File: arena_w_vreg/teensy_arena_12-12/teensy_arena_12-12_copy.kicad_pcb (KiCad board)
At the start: 4 copper layers, 254 x 254 mm, 87 parts, among them J1 Barrel_Jack, J2 Conn_01x04, J3 Conn_01x04, P1 CONN15, P10 CONN15, P11 CONN15, P12 CONN15, P2 CONN15, P3 CONN15, P4 CONN15, P5 CONN15, P6 CONN15, P7 CONN15, P8 CONN15, P9 CONN15, Q2 MOSFET_NCHAN, SW1 SW_SPDT, U1 TXB0108PW, U10 AZ1084-5.0, U11 AZ1084-5.0, U12 AZ1084-5.0, U13 AZ1084-5.0, U14 AZ1084-5.0, U15 AZ1084-5.0, U16 AZ1084-5.0, U17 AZ1084-5.0, U18 Teensy4.1, U2 TXB0108PW, U3 TXB0108PW, U4 TXB0108PW, U5 TXB0108PW, U6 AZ1084-5.0, U7 AZ1084-5.0, U8 AZ1084-5.0, U9 AZ1084-5.0

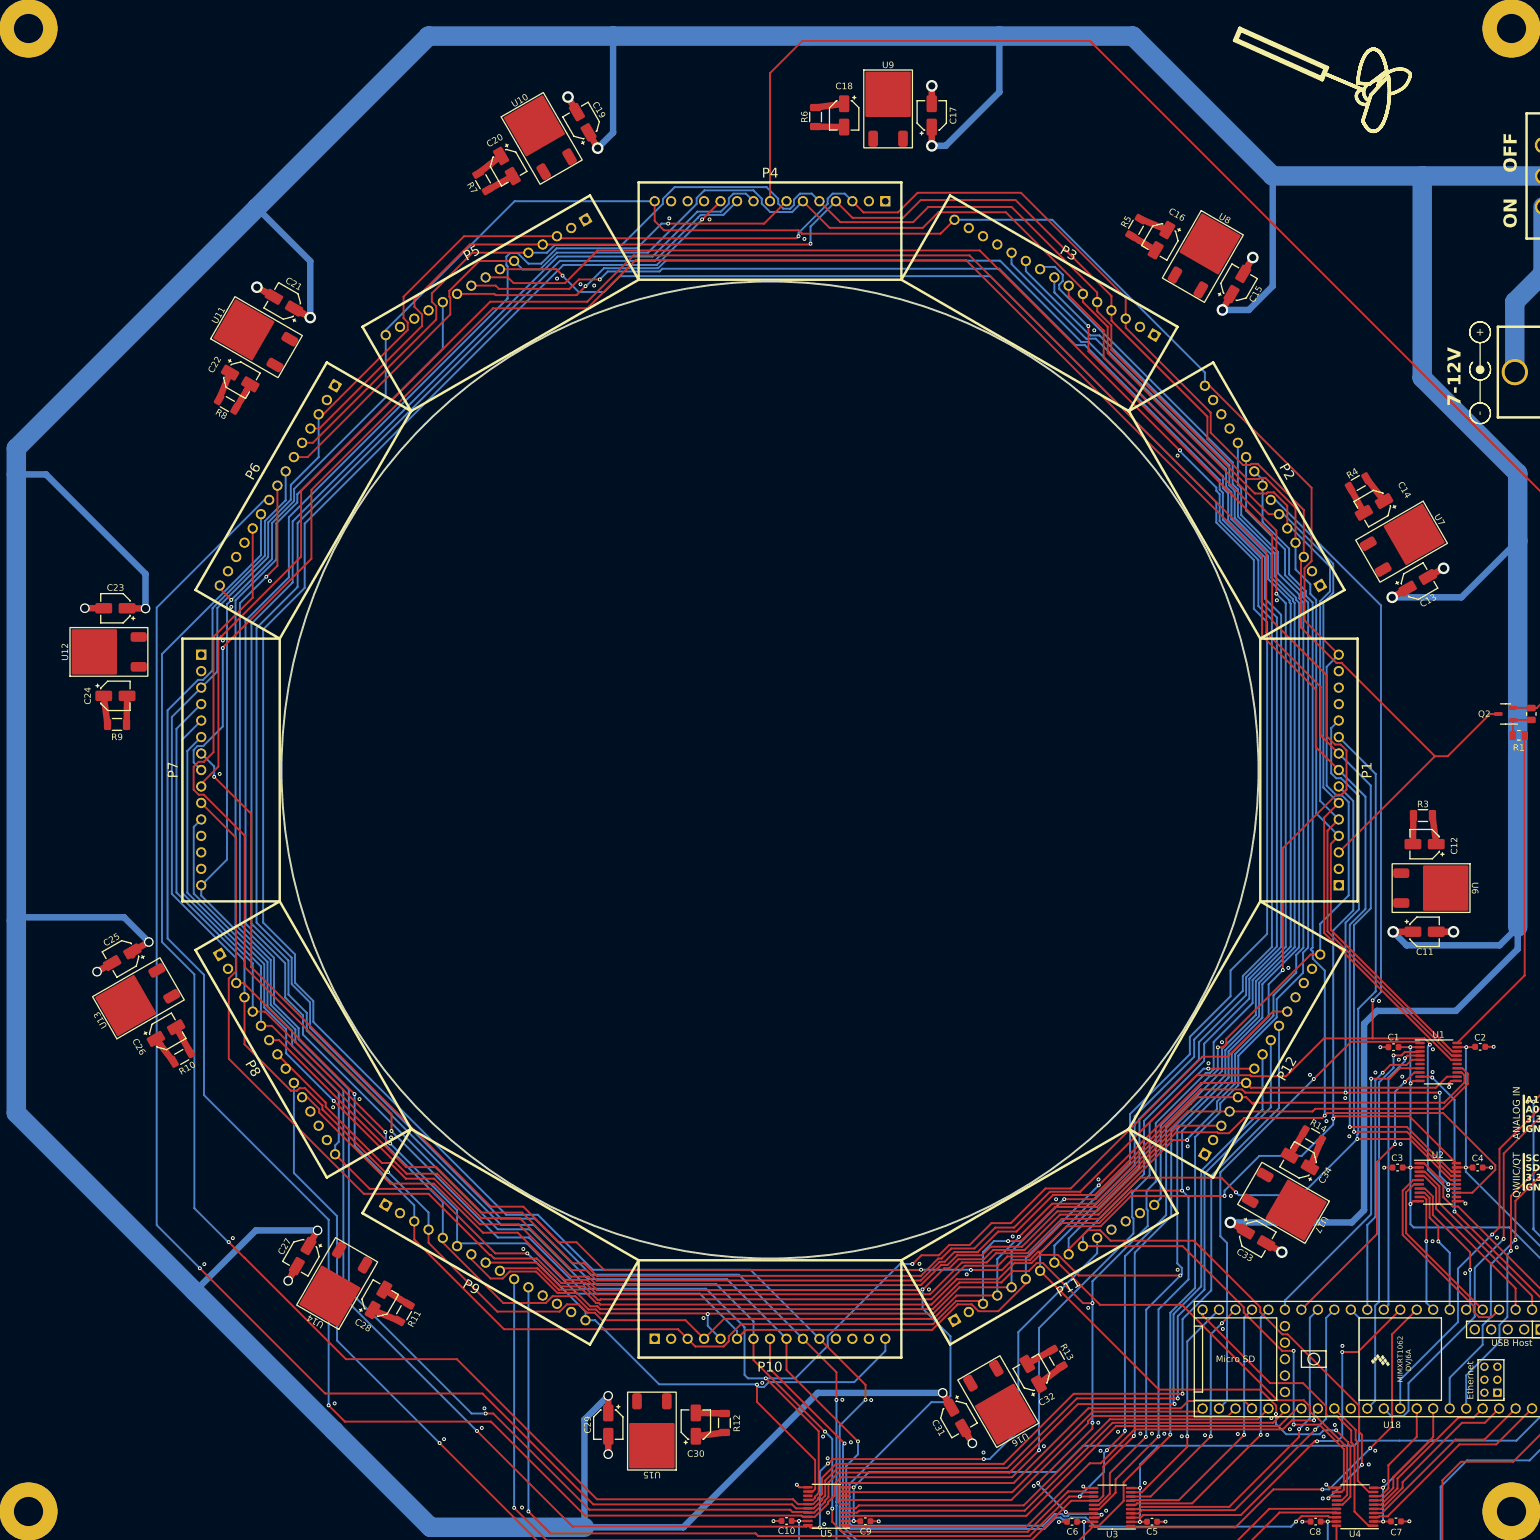
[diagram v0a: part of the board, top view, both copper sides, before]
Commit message: Fixed issue with AZ1084CD-5.0TRG1.
Note, need to do re-route the voltage regulators and redo the CPL file and gerber files.
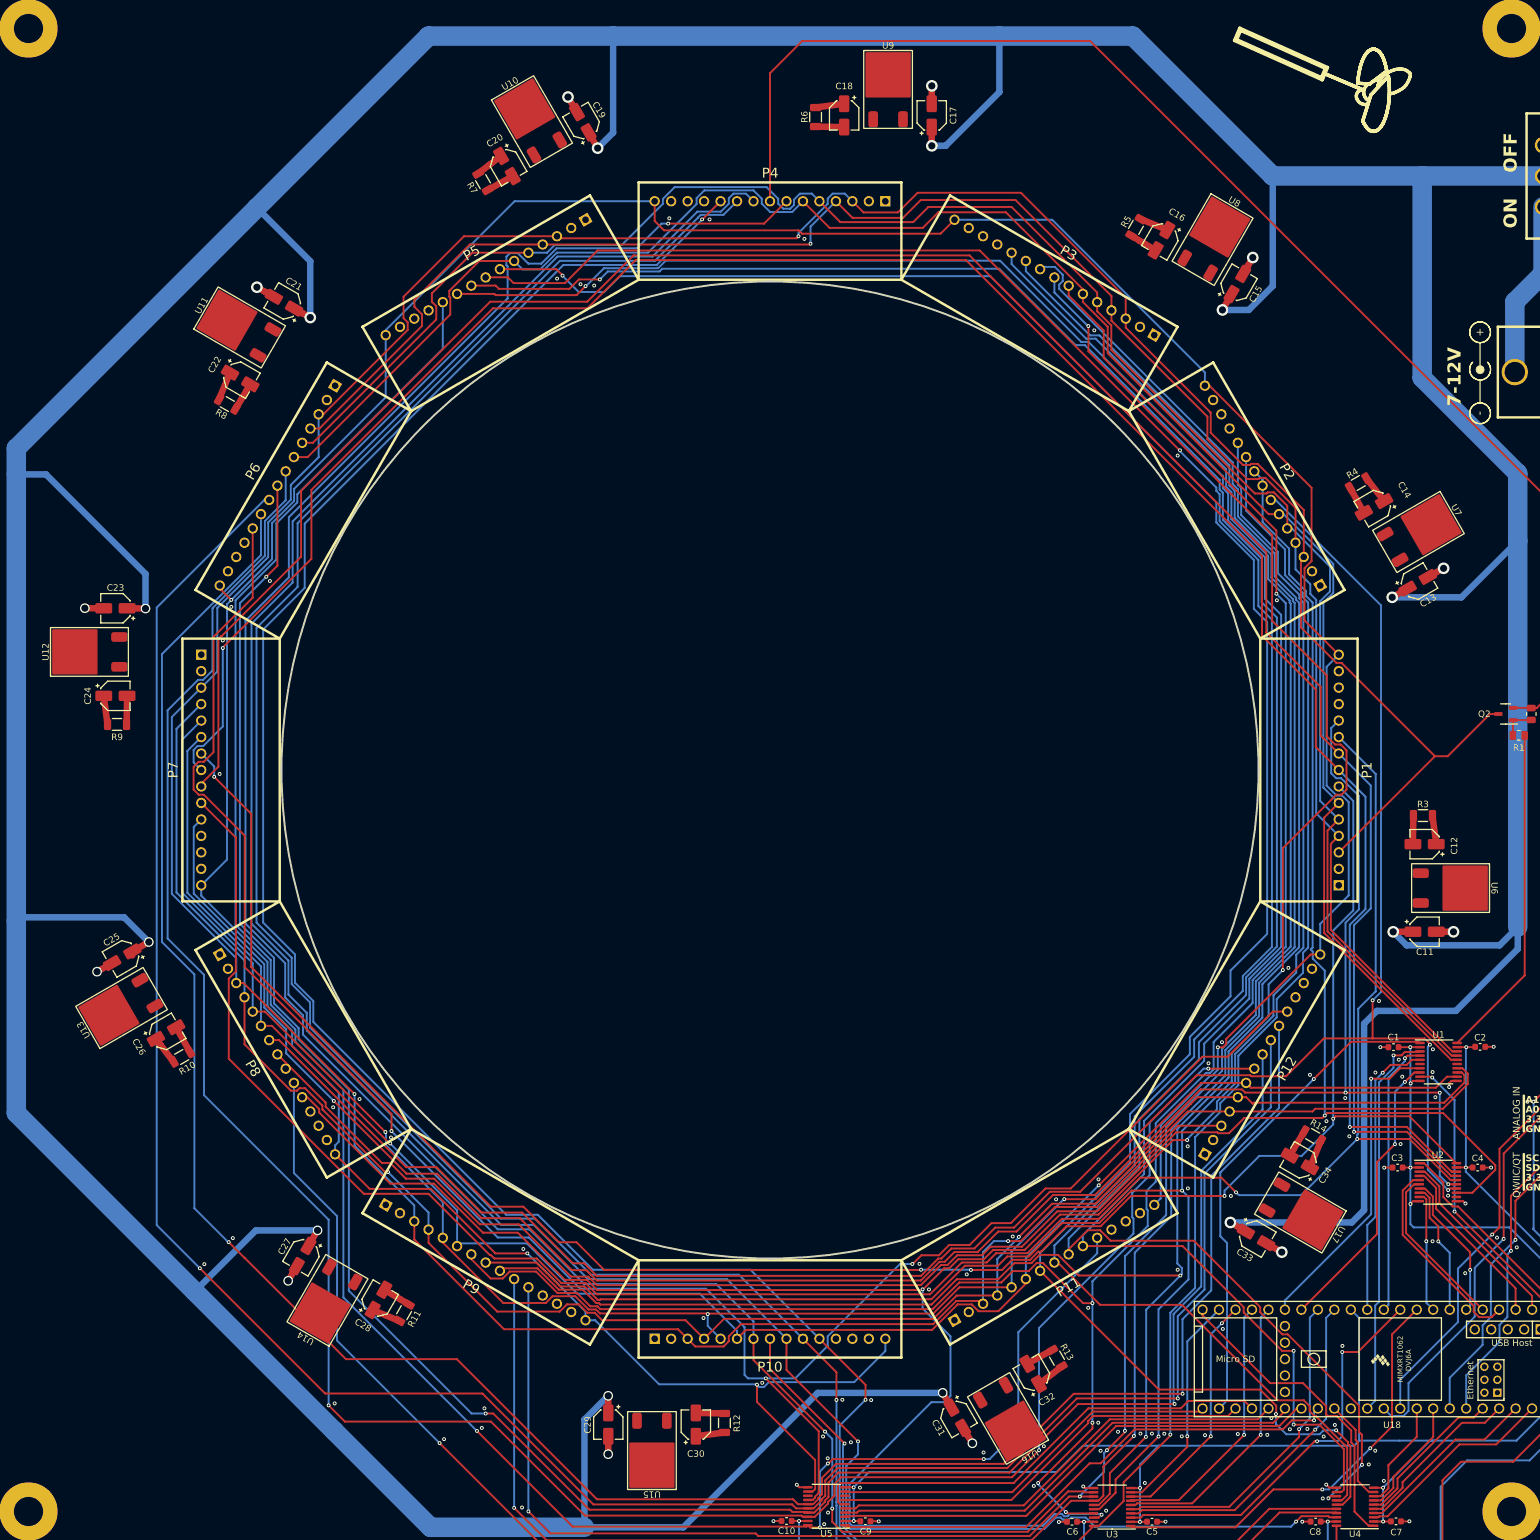
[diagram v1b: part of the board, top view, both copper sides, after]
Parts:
- moved U16 3.00 mm to (214.0, 276.8)
- moved U7 3.00 mm to (276.8, 141.6)
- moved U13 3.00 mm to (78.8, 214.0)
- moved U10 3.00 mm to (141.6, 78.8)
- moved U17 3.00 mm to (258.6, 245.5)
- moved U14 3.00 mm to (110.1, 258.6)
- moved U8 3.00 mm to (245.5, 97.0)
- moved U11 3.00 mm to (97.0, 110.1)
- moved U15 3.00 mm to (159.6, 281.7)
- moved U6 3.00 mm to (281.7, 196.0)
- moved U12 3.00 mm to (73.9, 159.6)
- moved U9 3.00 mm to (196.0, 73.9)
